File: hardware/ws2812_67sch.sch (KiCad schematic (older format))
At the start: 64 parts

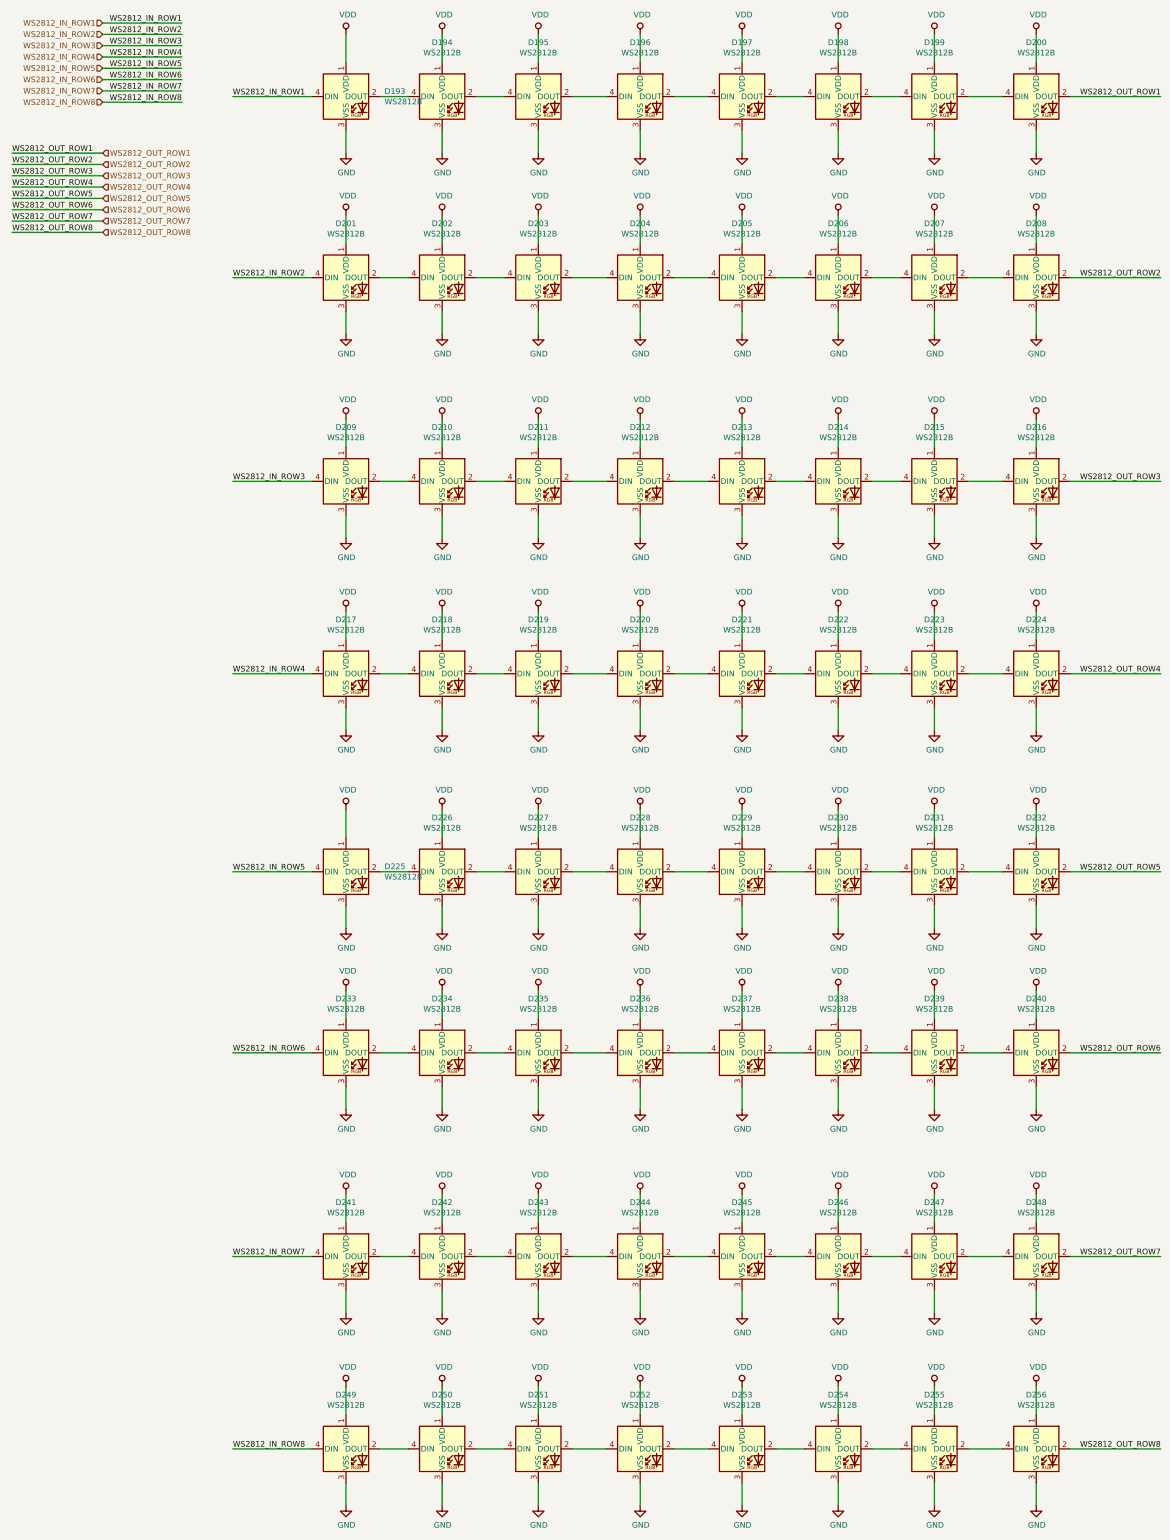
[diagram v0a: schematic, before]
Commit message: update WS2812\,
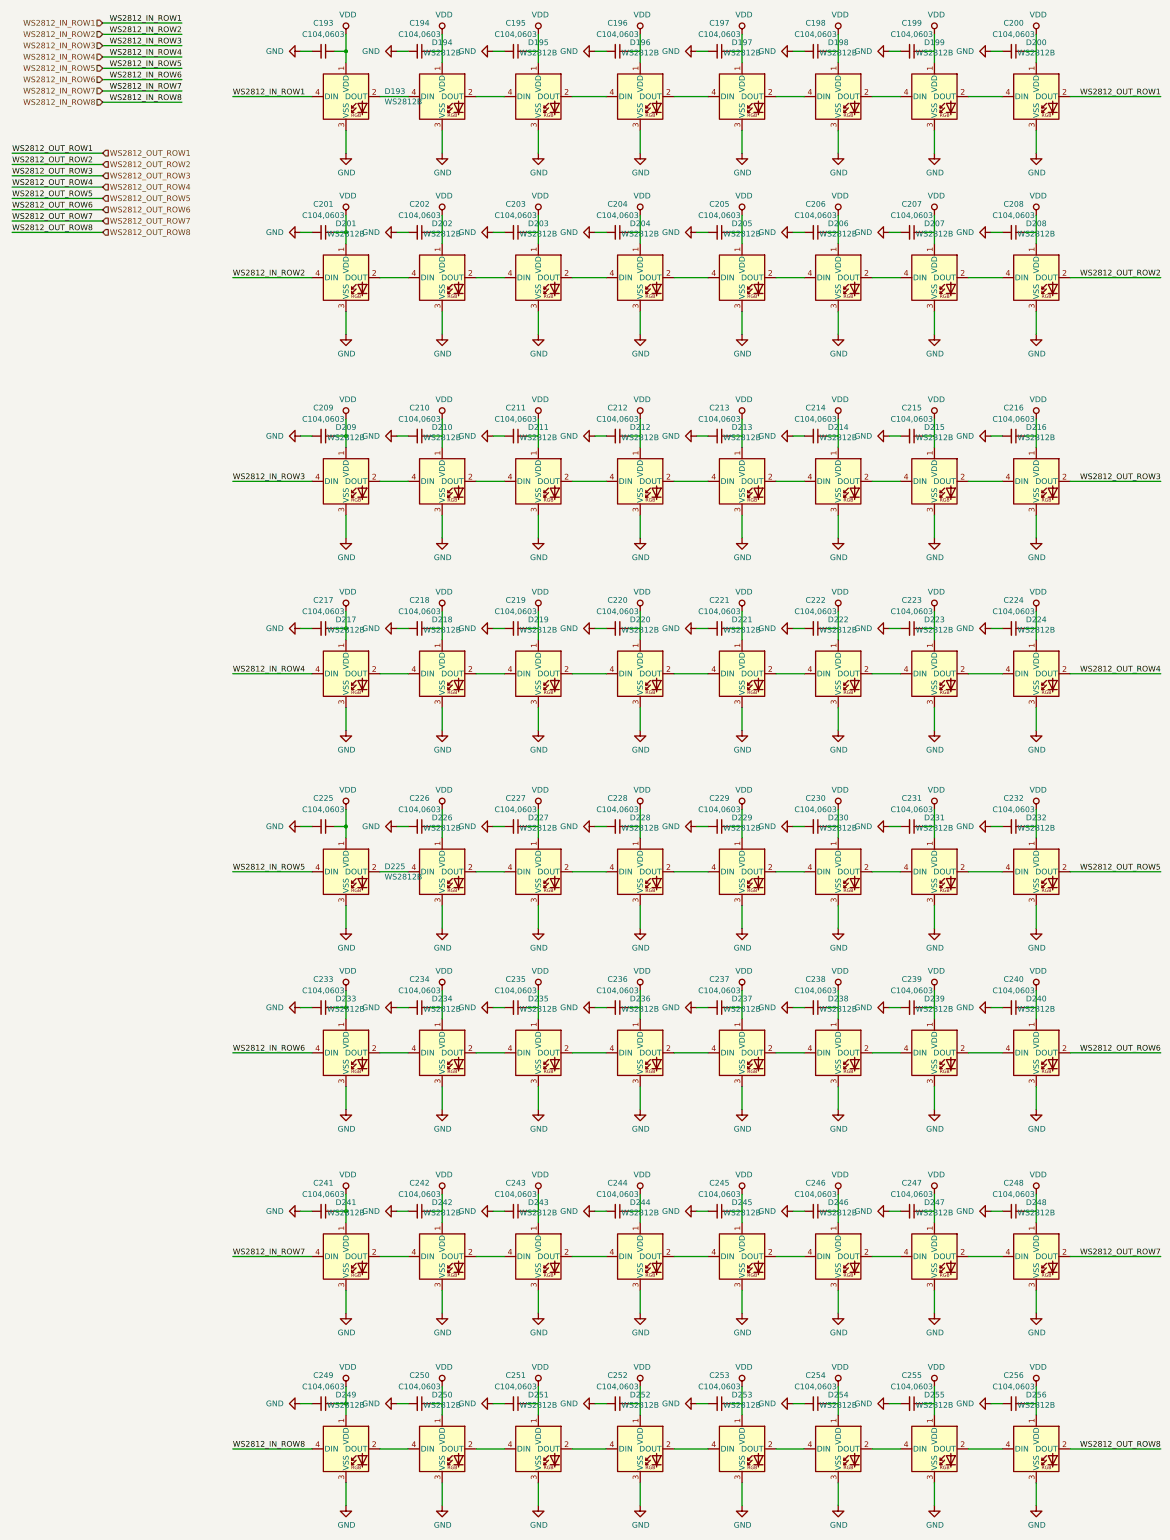
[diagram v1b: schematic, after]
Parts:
- added C193, C194, C195, C196, C197, C198, C199, C200, C201, C202, C203, C204, C205, C206, C207, C208, C209, C210, C211, C212, C213, C214, C215, C216, C217, C218, C219, C220, C221, C222, C223, C224, C225, C226, C227, C228, C229, C230, C231, C232, C233, C234, C235, C236, C237, C238, C239, C240, C241, C242, C243, C244, C245, C246, C247, C248, C249, C250, C251, C252, C253, C254, C255, C256: C104,0603, Capacitor_SMD:C_0603_1608Metric_Pad1.05x0.95mm_HandSolder, symbol taobao-c:C104,0603
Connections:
- wire segments 216 -> 352
